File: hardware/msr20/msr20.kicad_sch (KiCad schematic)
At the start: 18 parts, among them J1 Conn_Coaxial, U1 RF-BPF, U2 BGA616, U3 ADE-1+, U4 AD7478, U5 Pico

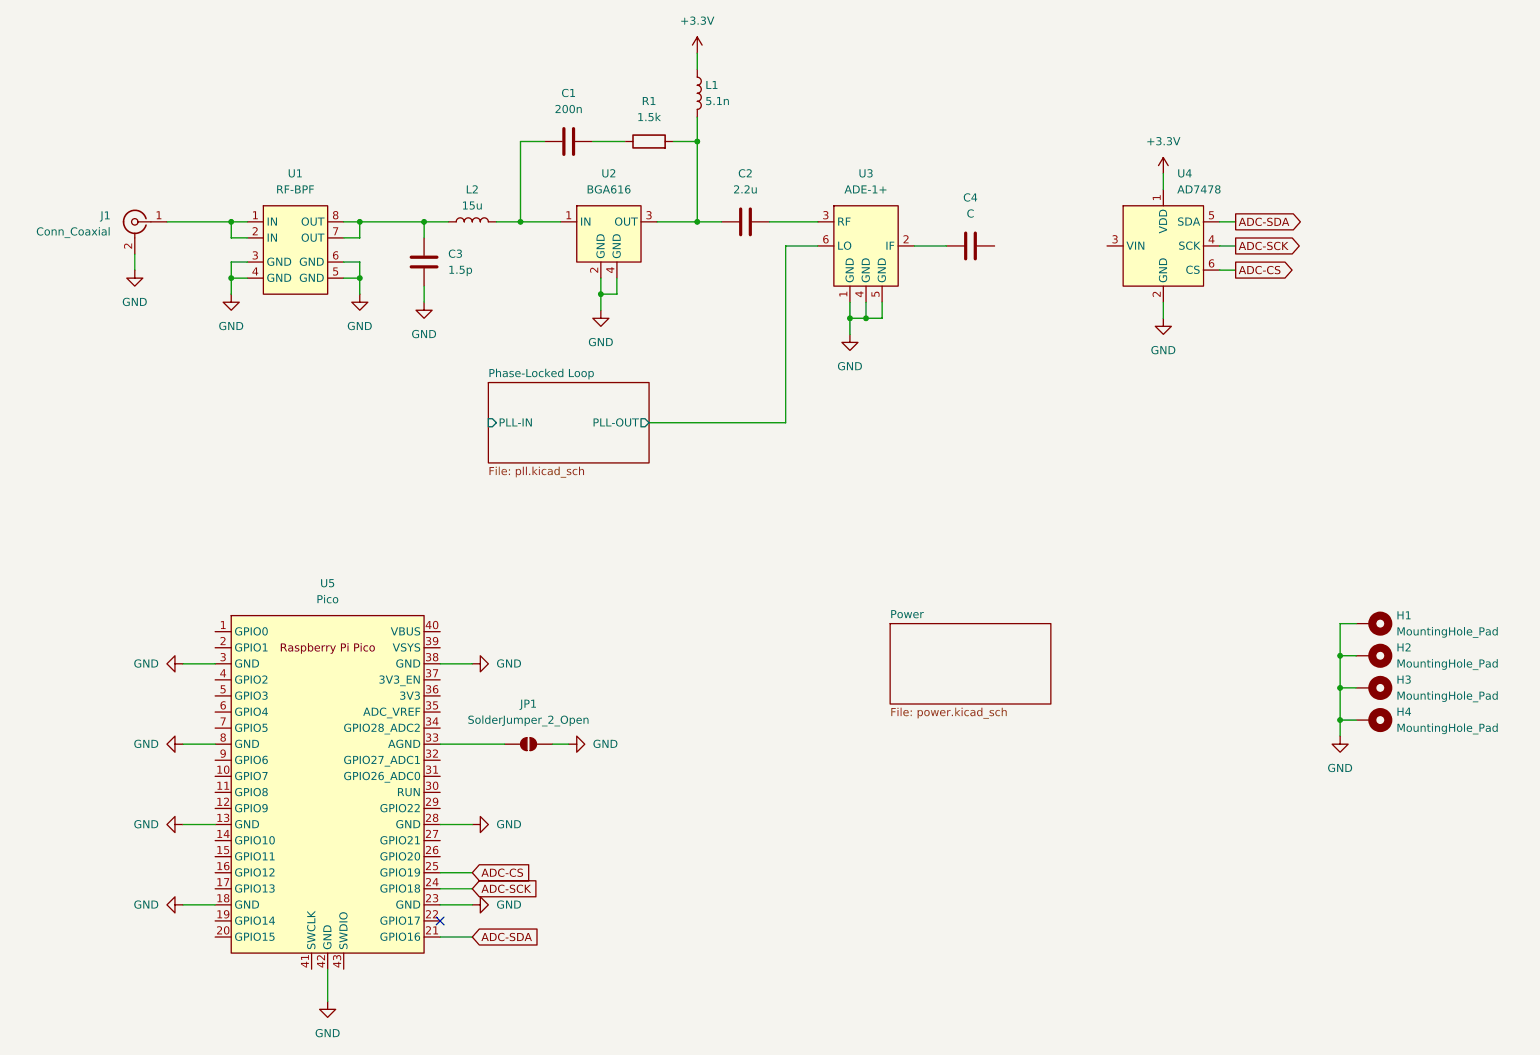
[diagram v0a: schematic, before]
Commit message: add if filter and if amplifier to schematic, organize into sheet hierarchy
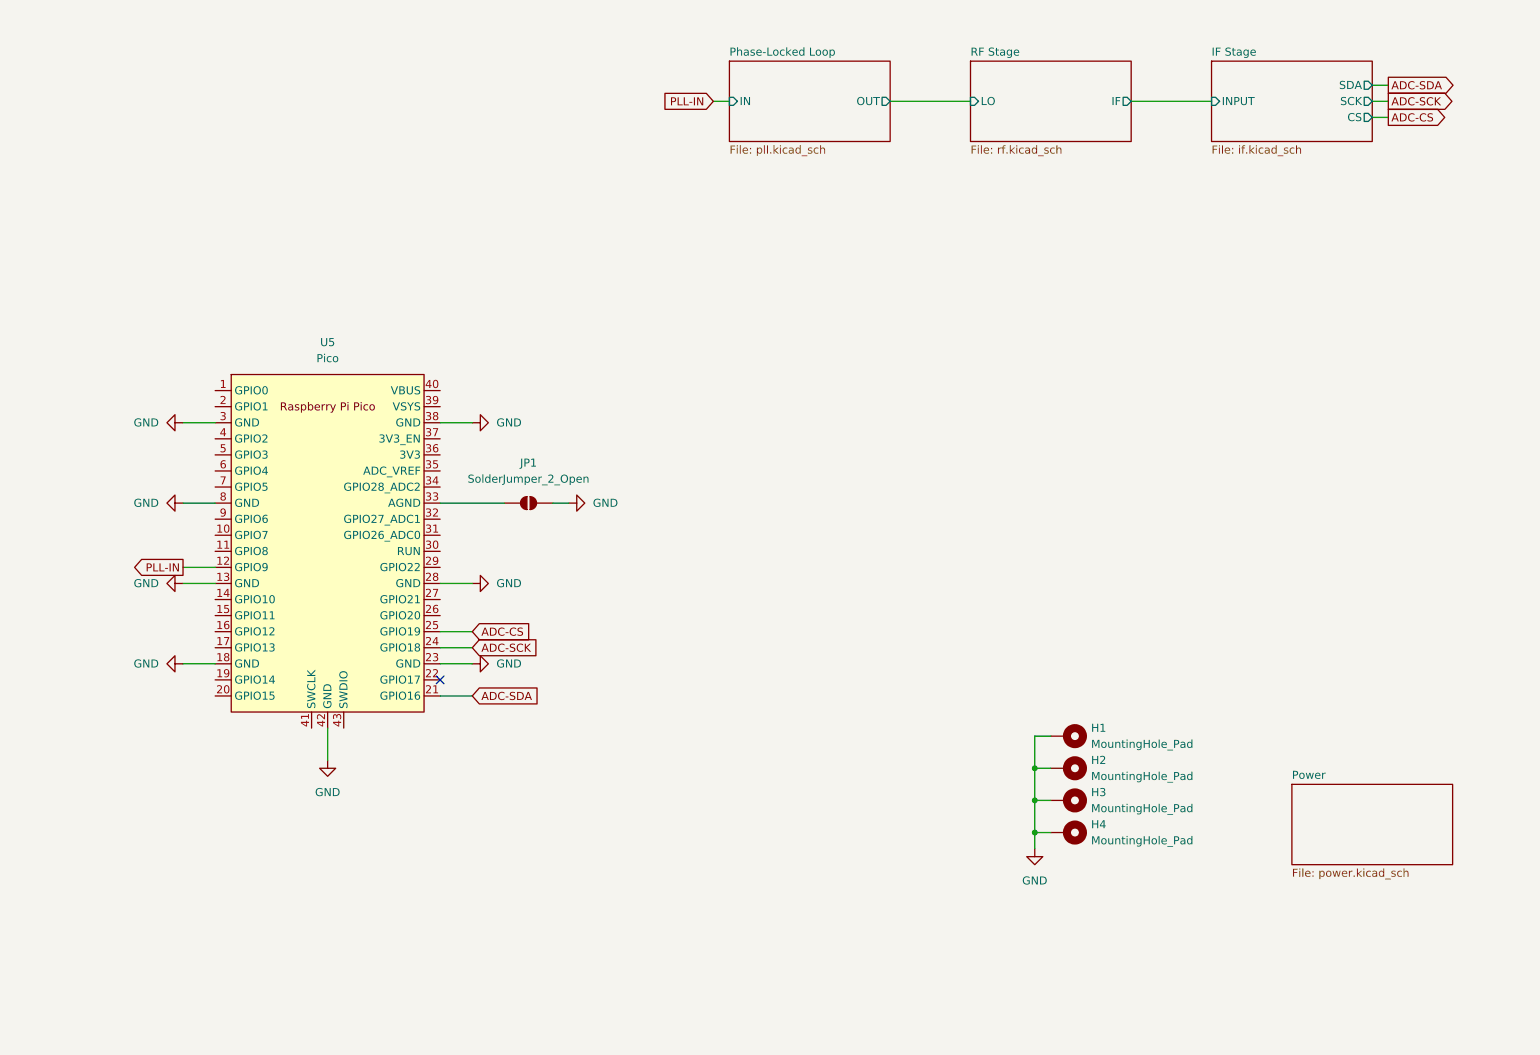
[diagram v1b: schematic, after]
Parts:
- removed C1: 200n, Capacitor_SMD:C_0805_2012Metric, symbol Device:C
- removed C2: 2.2u, Capacitor_SMD:C_0805_2012Metric, symbol Device:C
- removed C3: 1.5p, Capacitor_SMD:C_0805_2012Metric, symbol Device:C
- removed C4: C, Capacitor_SMD:C_0805_2012Metric, symbol Device:C
- removed J1: Conn_Coaxial, Connector_Coaxial:BNC_Amphenol_B6252HB-NPP3G-50_Horizontal, symbol Connector:Conn_Coaxial
- removed L1: 5.1n, Inductor_SMD:L_0805_2012Metric, symbol Device:L
- removed L2: 15u, Inductor_SMD:L_0805_2012Metric, symbol Device:L
- removed R1: 1.5k, Resistor_SMD:R_0805_2012Metric, symbol Device:R
- removed U1: RF-BPF, msr20:RF-BPF, symbol msr20:RF-BPF
- removed U2: BGA616, msr20:BGA616, symbol msr20:BGA616
- removed U3: ADE-1+, RF_Mini-Circuits:Mini-Circuits_CD636_H4.11mm, symbol msr20:ADE-1+
- removed U4: AD7478, Package_TO_SOT_SMD:SOT-23-6, symbol msr20:AD7478
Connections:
- net PLL-IN: now reaches U5.12 (GPIO9)
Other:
- added sheet IF Stage (if.kicad_sch)
- added sheet RF Stage (rf.kicad_sch)
- sheet Phase-Locked Loop ports: added IN, OUT; removed PLL-IN, PLL-OUT
- moved on the sheet: H1, H2, H3, H4, JP1, U5
